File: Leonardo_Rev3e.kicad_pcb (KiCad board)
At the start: 2 copper layers, 68.6 x 53.3 mm, 61 parts, among them IC1 REG1117-5, IC2 LMV358IDGKR, J1 USBMICRO, J2 8x1F-H8.5, J3 8x1F-H8.5, J4 6x1F-H8.5, T1 FDN340P, U1 ATMEGA32U4-XUMU, U2 ATMEGA32U4-XUAU, U3 LP2985-33DBVR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

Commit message: feat: resize all references/text and match pin markings
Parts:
- moved REF** 2.97 mm to (143.3, 90.4)
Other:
- board text added: "- PWM〜"
- board text added: "LEONARDO"
- board text added: "POWER"
- board text added: "Vin"
- board text added: "〜10"
- board text added: "〜11"
- board text added: "〜13"
- board text added: "〜3"
- board text added: "〜5"
- board text added: "〜6"
- board text added: "〜9"
- board text removed: "#"
- board text removed: "+3.3V"
- board text removed: "+5V"
- board text removed: "10"
- board text removed: "11"
- board text removed: "13"
- board text removed: "3"
- board text removed: "5"
- board text removed: "6"
- board text removed: "9"
- board text removed: "VIN"
- board text removed: "[#=PWM]"

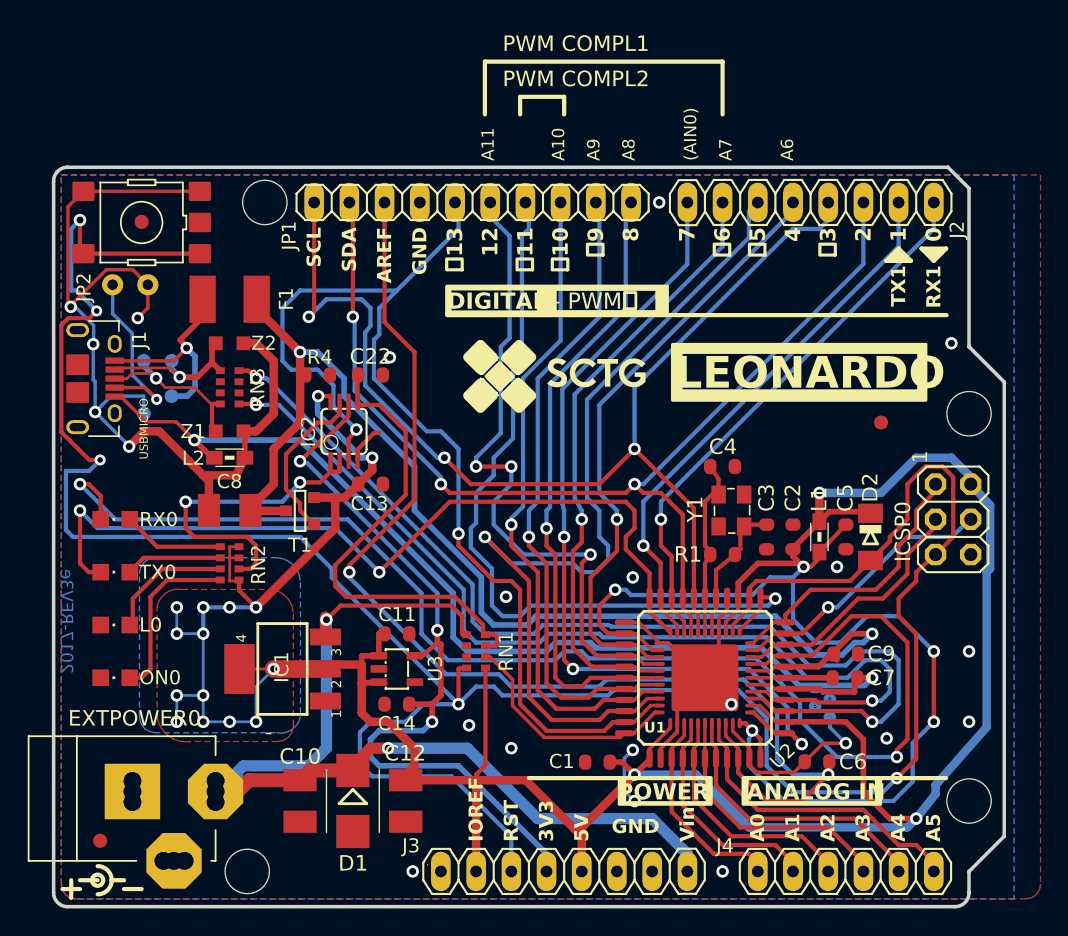
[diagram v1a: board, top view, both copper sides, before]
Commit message: chore: clean up footprint library
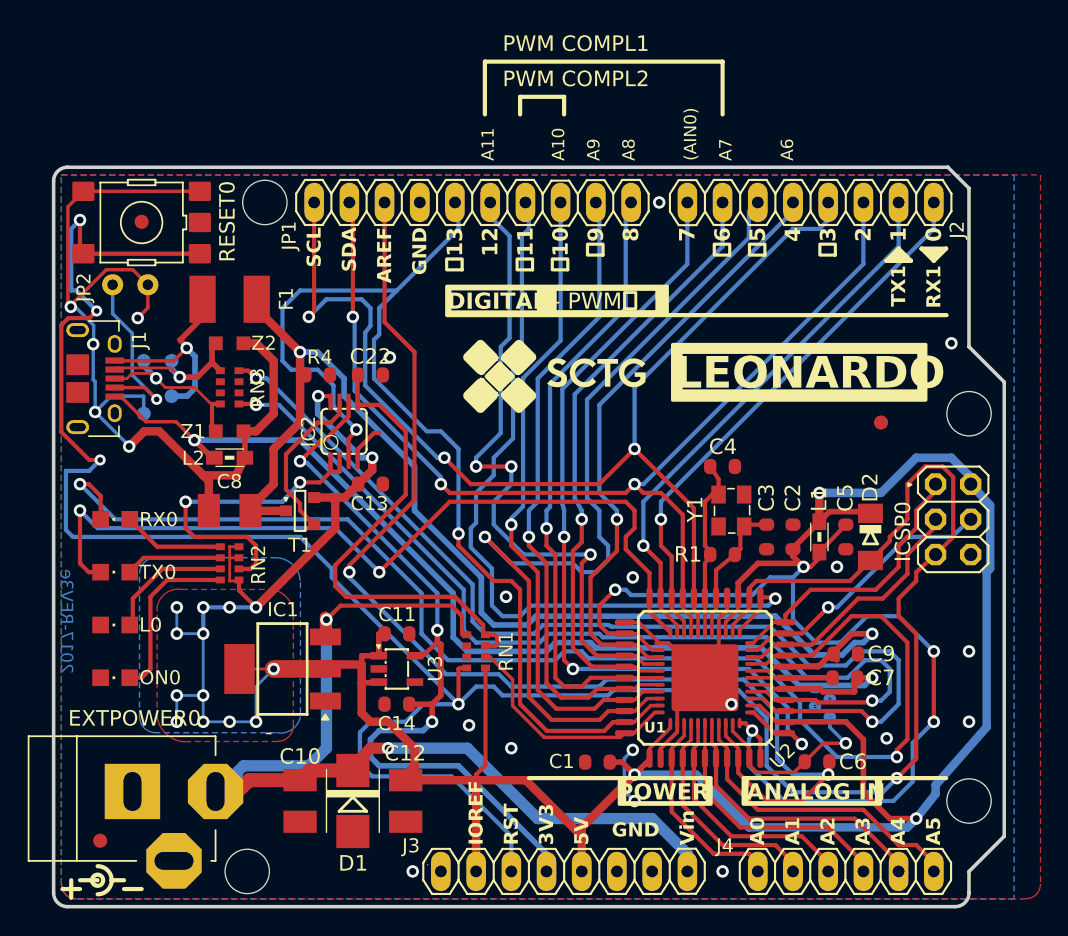
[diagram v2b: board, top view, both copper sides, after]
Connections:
- net COM renamed 3x2M_NM
- net GND1 renamed UGND
